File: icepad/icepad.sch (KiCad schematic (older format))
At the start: 40 parts

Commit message: added mcu
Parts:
- added U?: STM32F042F6Px, Package_SO:TSSOP-20_4.4x6.5mm_P0.65mm, symbol MCU_ST_STM32F0:STM32F042F6Px
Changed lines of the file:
@@
 EESchema Schematic File Version 4
+LIBS:icepad-cache
 EELAYER 30 0
 EELAYER END
@@
 	1    0    0    -1
 $EndComp
+$Comp
+L MCU_ST_STM32F0:STM32F042F6Px U?
+U 1 1 5E43D887
+P 3600 3000
+F 0 "U?" H 3600 2111 50  0000 C CNN
+F 1 "STM32F042F6Px" H 3600 2020 50  0000 C CNN
+F 2 "Package_SO:TSSOP-20_4.4x6.5mm_P0.65mm" H 3100 2300 50  0001 R CNN
+F 3 "http://www.st.com/st-web-ui/static/active/en/resource/technical/document/datasheet/DM00105814.pdf" H 3600 3000 50  0001 C CNN
+	1    3600 3000
+	1    0    0    -1
+$EndComp
+Text GLabel 4500 3300 2    50   BiDi ~ 0
+USB_DM
+Text GLabel 4500 3400 2    50   BiDi ~ 0
+USB_DP
 $EndSCHEMATC

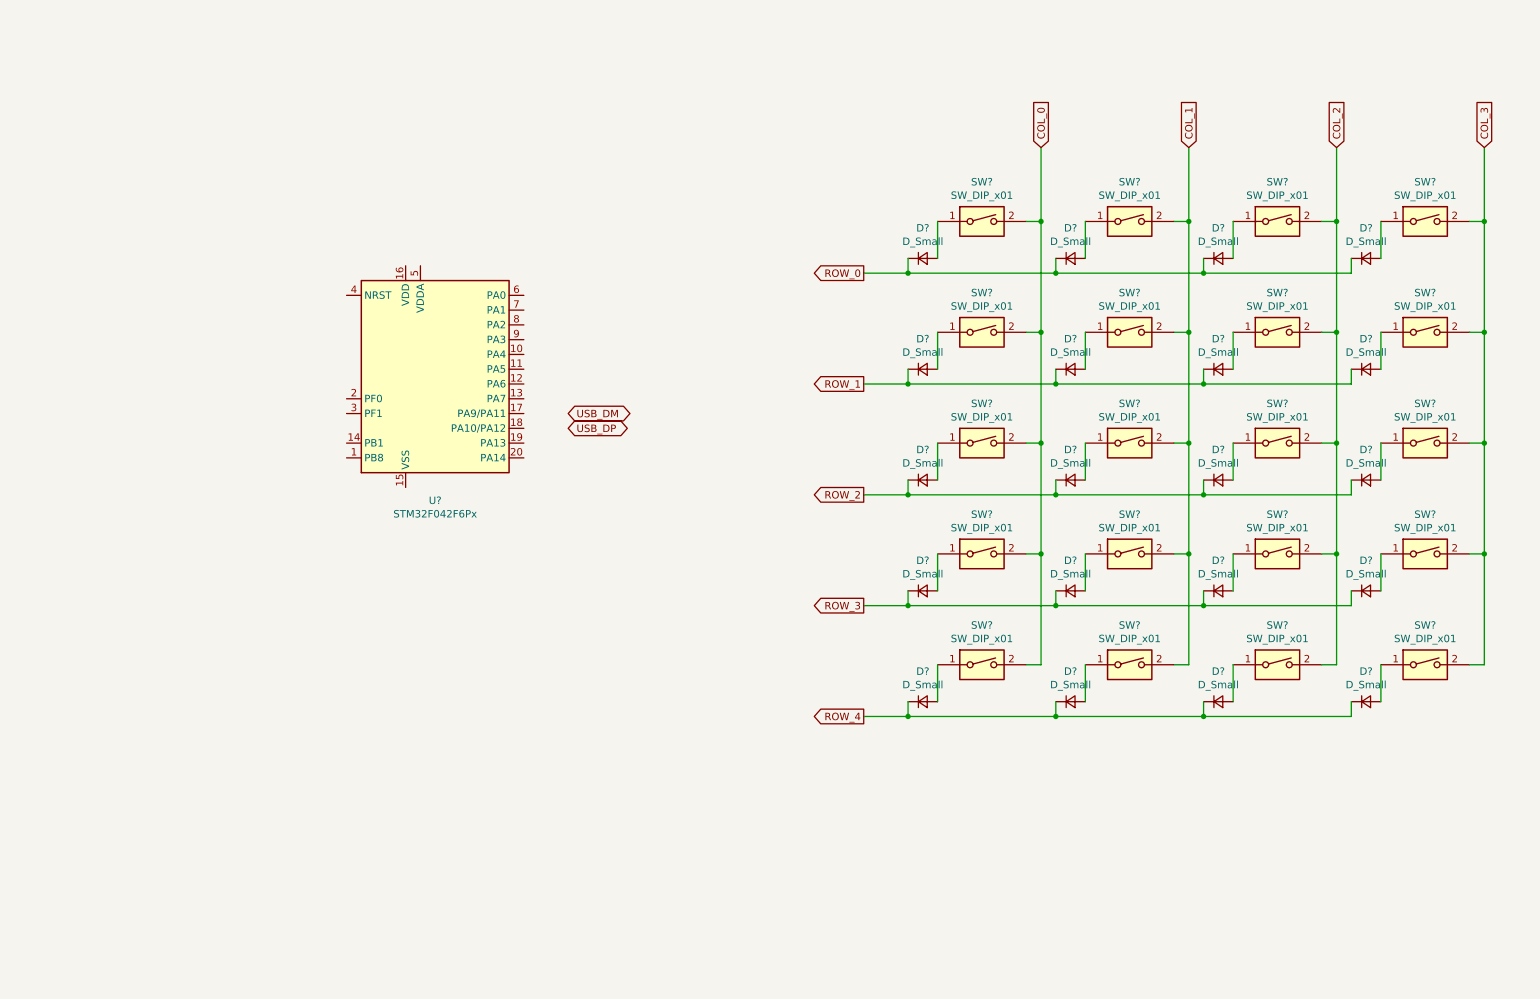
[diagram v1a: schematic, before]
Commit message: removed old submodule
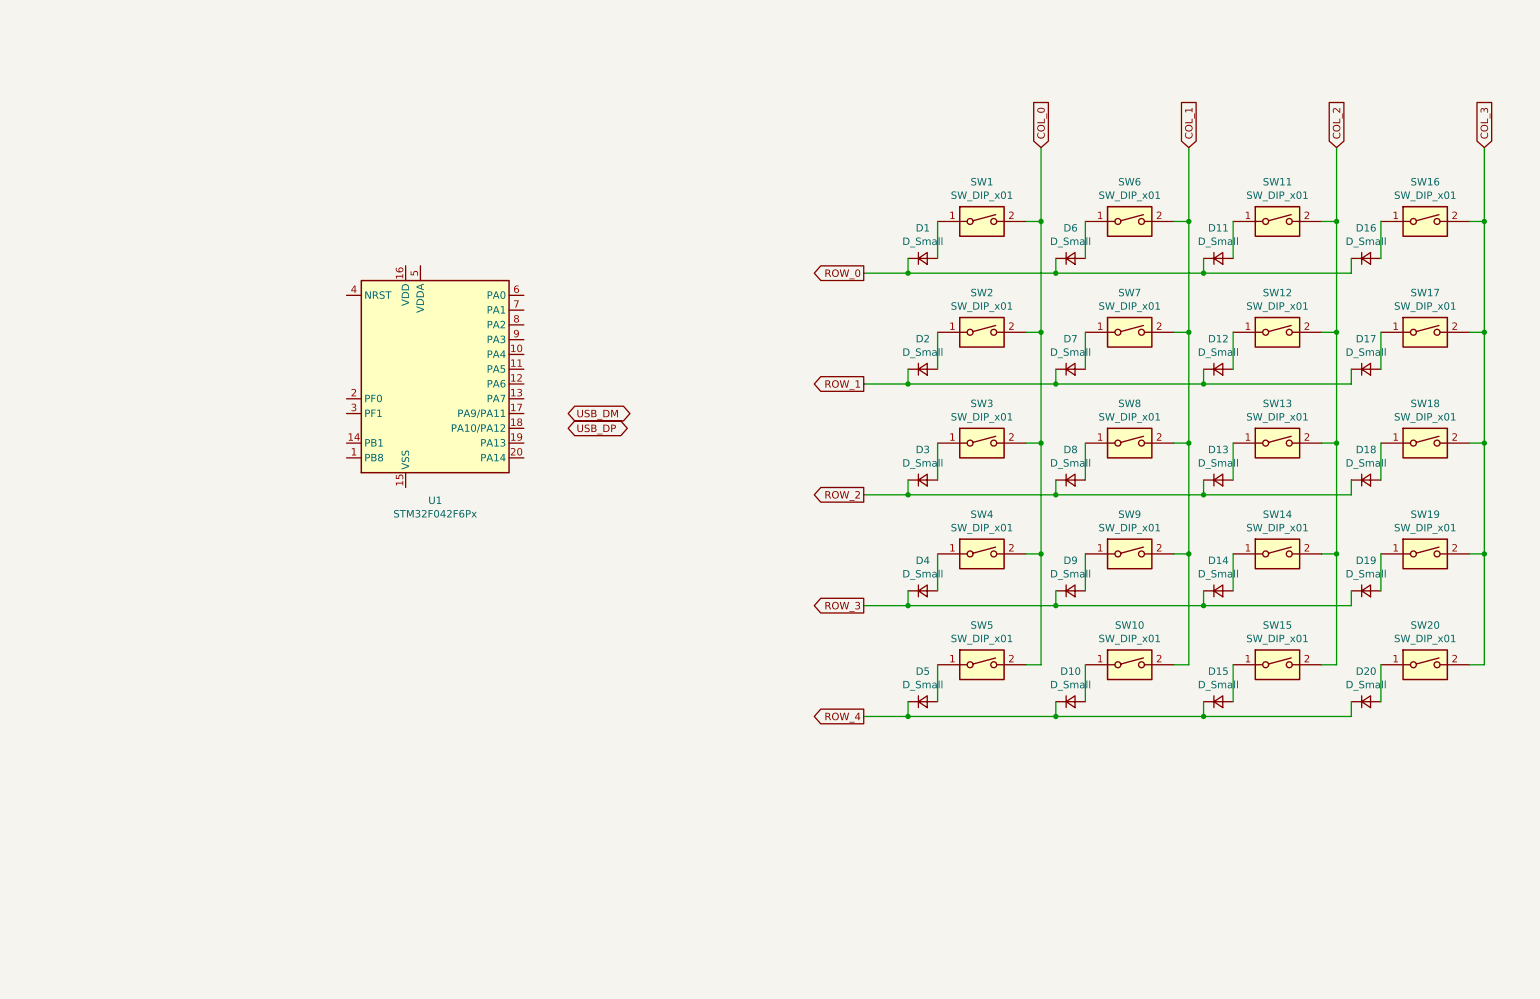
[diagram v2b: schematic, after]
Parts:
- SW1, SW10, SW11, SW12, SW13, SW14, SW15, SW16, SW17, SW18, SW19, SW2, SW20, SW3, SW4, SW5, SW6, SW7, SW8, SW9: renamed from SW?; footprint (none) -> keyswitches:Kailh_socket_MX
- gave numbers to parts that had none: 21

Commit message: schematic edits
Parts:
- removed D1, D10, D11, D12, D13, D14, D15, D16, D17, D18, D19, D2, D20, D3, D4, D5, D6, D7, D8, D9: D_Small, symbol Device:D_Small
- removed SW1, SW10, SW11, SW12, SW13, SW14, SW15, SW16, SW17, SW18, SW19, SW2, SW20, SW3, SW4, SW5, SW6, SW7, SW8, SW9: SW_DIP_x01, keyswitches:Kailh_socket_MX, symbol Switch:SW_DIP_x01
- added D? (x16): D_Small, symbol Device:D_Small
- added MX? (x16): MX-LED, symbol MX_Alps_Hybrid:MX-LED
- added R? (x2): 5k1, symbol Device:R_Small
- added USB?: Wurth-632723300011, symbol Type-C:Wurth-632723300011
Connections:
- new net: D?.2 (A), MX?.2 (ROW) (x16)
- new net: R?.2, USB?.17 (CC2)
- new net: R?.2, USB?.5 (CC1)
- new net Col_0_Key: MX?.1 (COL), MX?.1 (COL), MX?.1 (COL), MX?.1 (COL)
- new net Col_0_LED: MX?.3 (LED), MX?.3 (LED), MX?.3 (LED), MX?.3 (LED)
- new net Col_1_Key: MX?.1 (COL), MX?.1 (COL), MX?.1 (COL), MX?.1 (COL)
- new net Col_1_LED: MX?.3 (LED), MX?.3 (LED), MX?.3 (LED), MX?.3 (LED)
- new net Col_2_Key: MX?.1 (COL), MX?.1 (COL), MX?.1 (COL), MX?.1 (COL)
- new net Col_2_LED: MX?.3 (LED), MX?.3 (LED), MX?.3 (LED), MX?.3 (LED)
- new net Col_3_Key: MX?.1 (COL), MX?.1 (COL), MX?.1 (COL), MX?.1 (COL)
- new net Col_3_LED: MX?.3 (LED), MX?.3 (LED), MX?.3 (LED), MX?.3 (LED)
- new net DN: USB?.19 (Dn2), USB?.7 (Dn1)
- new net DP: USB?.18 (Dp2), USB?.6 (Dp1)
- new net GND: R?.1, R?.1, USB?.1 (GND), USB?.12 (GND), USB?.13 (GND), USB?.24 (GND), USB?.25 (Center_Plate_Pin), USB?.26 (Connector_Legs), USB?.27 (Under-Barrel_Pads)
- new net Row_0_Key: D?.1 (K), D?.1 (K), D?.1 (K), D?.1 (K)
- new net Row_0_LED: MX?.4 (LEDGND), MX?.4 (LEDGND), MX?.4 (LEDGND), MX?.4 (LEDGND)
- new net Row_1_Key: D?.1 (K), D?.1 (K), D?.1 (K), D?.1 (K)
- new net Row_1_LED: MX?.4 (LEDGND), MX?.4 (LEDGND), MX?.4 (LEDGND), MX?.4 (LEDGND)
- new net Row_2_Key: D?.1 (K), D?.1 (K), D?.1 (K), D?.1 (K)
- new net Row_2_LED: MX?.4 (LEDGND), MX?.4 (LEDGND), MX?.4 (LEDGND), MX?.4 (LEDGND)
- new net Row_3_Key: D?.1 (K), D?.1 (K), D?.1 (K), D?.1 (K)
- new net Row_3_LED: MX?.4 (LEDGND), MX?.4 (LEDGND), MX?.4 (LEDGND), MX?.4 (LEDGND)
- new net VBUS: USB?.16 (VBUS), USB?.21 (VBUS), USB?.4 (VBUS), USB?.9 (VBUS)
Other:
- moved on the sheet: U1

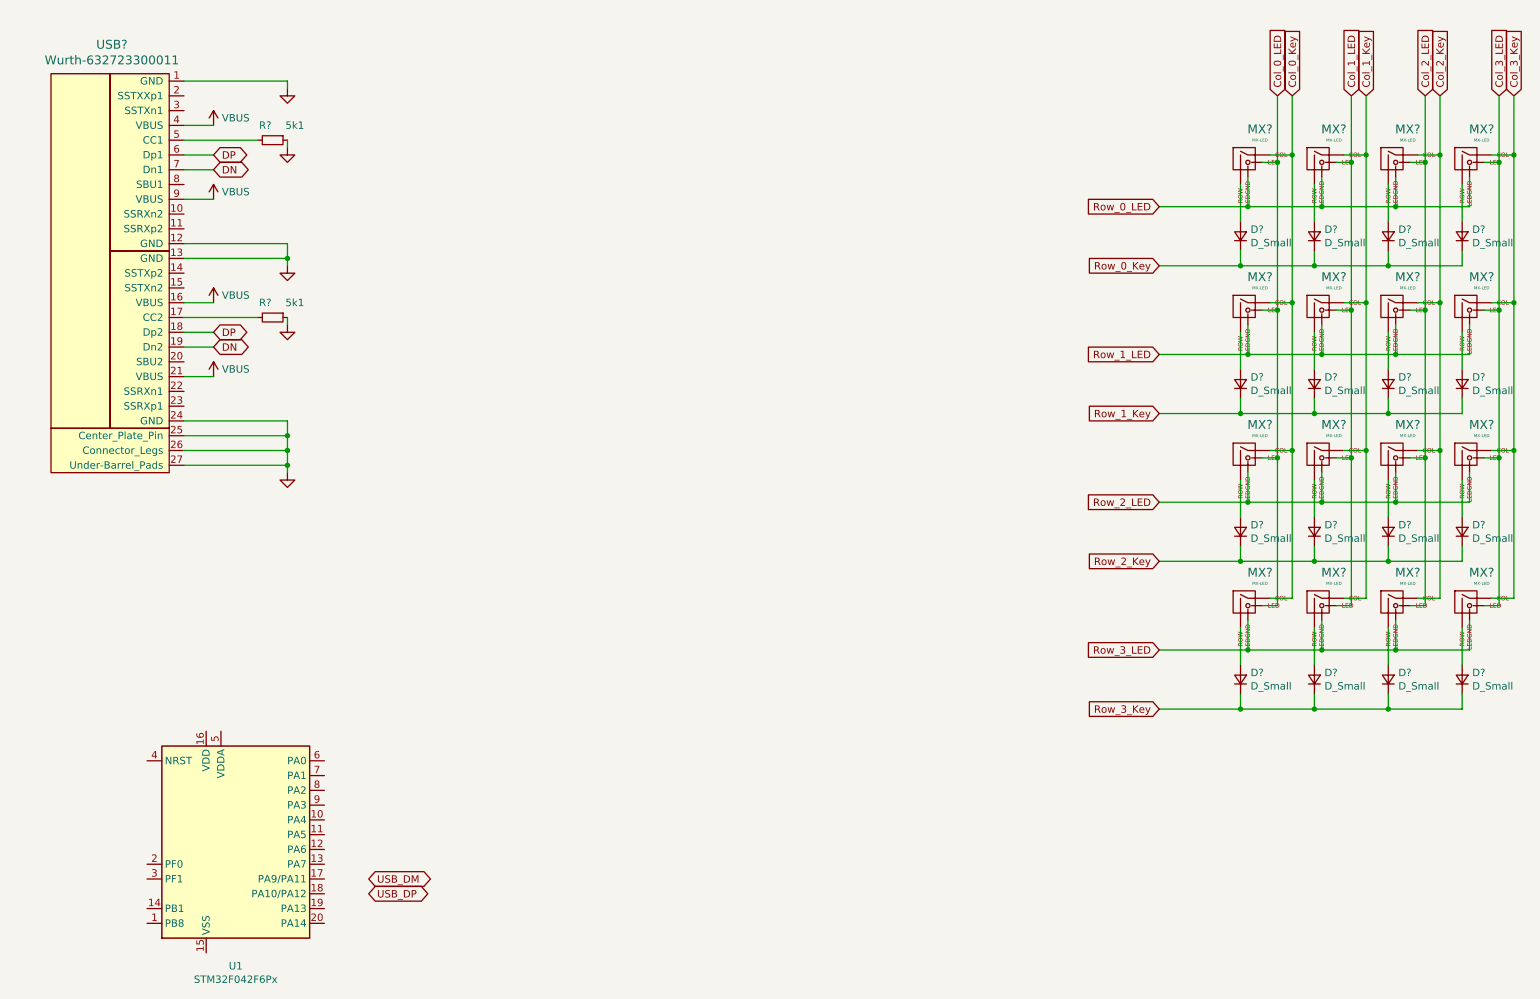
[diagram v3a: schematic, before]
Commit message: Added DC DC converter and decoupling caps for MCU
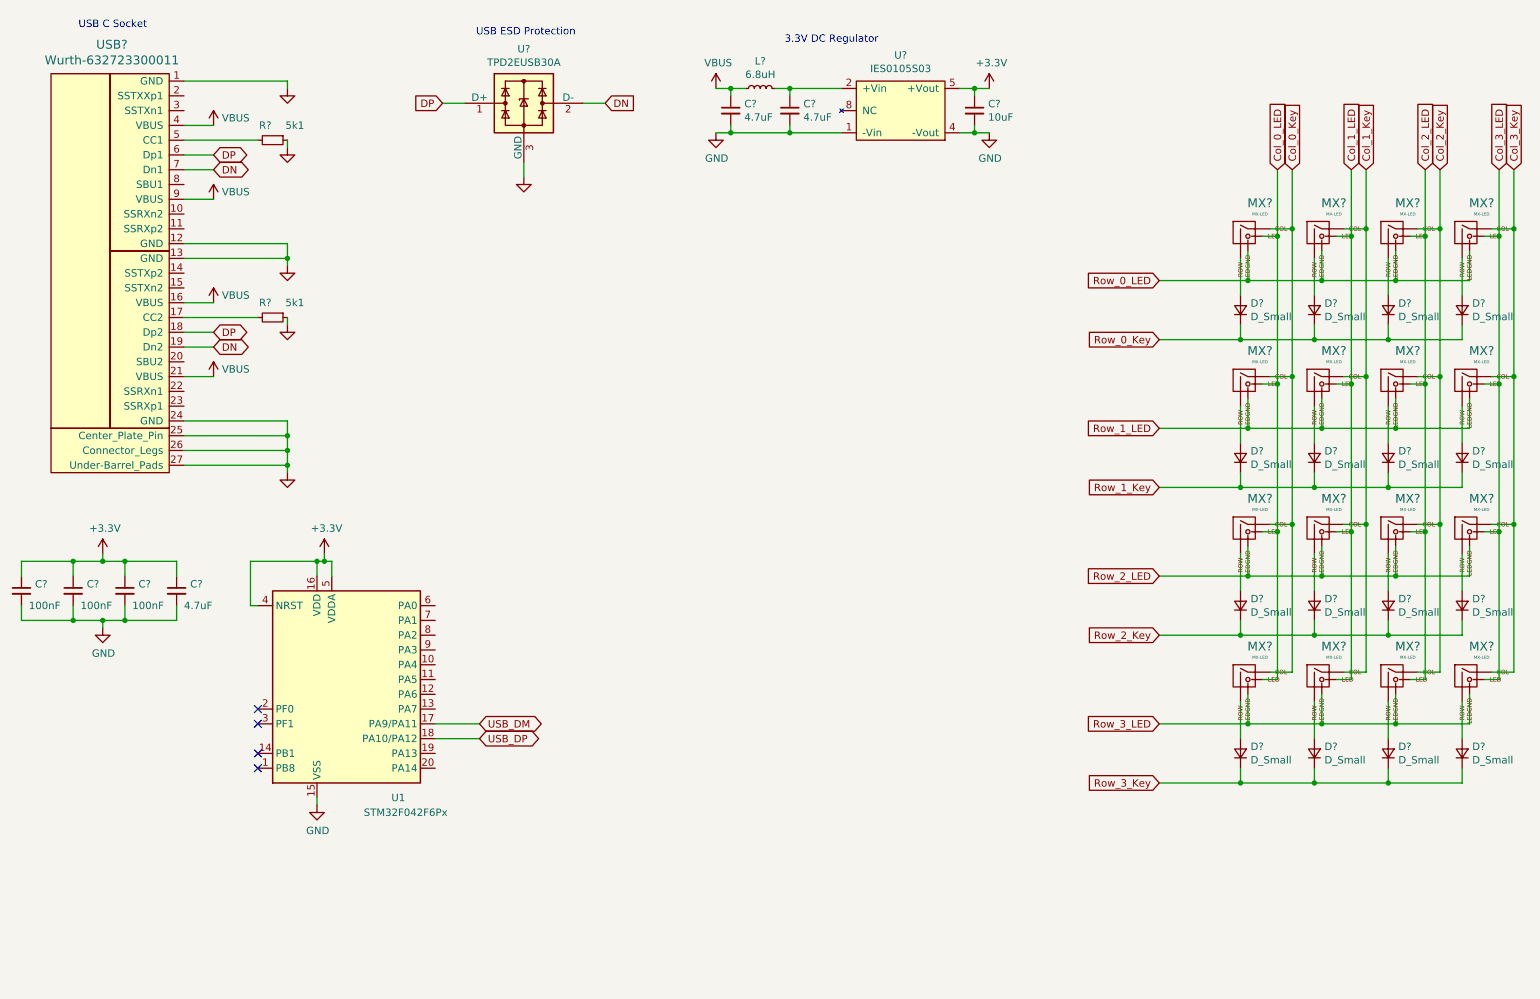
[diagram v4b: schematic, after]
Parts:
- added C? (x3): 4.7uF, symbol Device:C_Small
- added C?: 10uF, symbol Device:C_Small
- added C? (x3): 100nF, symbol Device:C_Small
- added L?: 6.8uH, symbol Device:L_Small
- added U?: TPD2EUSB30A, Package_TO_SOT_SMD:Texas_DRT-3, symbol Power_Protection:TPD2EUSB30A
- added U?: IES0105S03, symbol IES0105S03:IES0105S03
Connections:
- net DN: now also U?.2 (D-)
- net DP: now also U?.1 (D+)
- net GND: now also U1.15 (VSS), C?.2, C?.2, C?.2, C?.2, C?.2, C?.2, C?.2, U?.1 (-Vin), U?.3 (GND), U?.4 (-Vout)
- net USB_DM: now also U1.17 (PA9/PA11)
- net USB_DP: now also U1.18 (PA10/PA12)
- net VBUS: now also C?.1, L?.1
- net +3V3: now reaches U1.16 (VDD)
- net +3V3: now also U1.4 (NRST), U1.5 (VDDA), C?.1, C?.1, C?.1, C?.1, C?.1, U?.5 (+Vout)
- new net: C?.1, L?.2, U?.2 (+Vin)
- no-connect marks 0 -> 4
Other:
- note added: "3.3V DC Regulator"
- note added: "USB C Socket"
- note added: "USB ESD Protection"
- moved on the sheet: D?, MX?, U1
